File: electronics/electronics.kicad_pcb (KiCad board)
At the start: 2 copper layers, 50.3 x 40.6 mm, 24 parts, among them J3 EXTERNAL CONTROL, J4 POWER, J5 I2C BUS, J6 I2C BUS, J7 INPUT, J8 OUTPUT, U1 ProMicro

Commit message: Changed some art
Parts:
- removed svg2mod: G***, local:kv27v66mod
- removed svg2mod: G***, local:c6p-dev
- added c6p_logo: G***, local:c6p-dev, F.Cu at (120.1, 34.0)
- added kv_revision: G***, local:kv27v66mod, F.Cu at (110.5, 40.4)

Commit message: Last through hole
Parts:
- removed the REF** at (96.5, 54.4)
- removed the REF** at (138.2, 54.4)
- removed kv_revision: G***, local:kv27v66mod
- added REF**: MountingHole_3.2mm_M3_DIN965, MountingHole:MountingHole_3.2mm_M3_DIN965, F.Cu at (96.5, 54.4)
- R5, R6, R7, R8: footprint Resistor_THT:R_Axial_DIN0204_L3.6mm_D1.6mm_P1.90mm_Vertical -> Resistor_THT:R_Axial_DIN0204_L3.6mm_D1.6mm_P2.54mm_Vertical
- REF**: value MountingHole_3.2mm_M3 -> MountingHole_3.2mm_M3_DIN965; footprint MountingHole:MountingHole_3.2mm_M3 -> MountingHole:MountingHole_3.2mm_M3_DIN965
- moved J8 13.2 mm to (131.3, 50.5), turned to 0 degrees
- moved R8 12.9 mm to (135.6, 22.9)
- moved C4 9.88 mm to (140.0, 28.4)
- moved C1 8.20 mm to (129.3, 36.1)
- moved C2 8.20 mm to (134.1, 36.1)
- moved c6p_logo 7.16 mm to (113.8, 37.3)
- moved R7 4.35 mm to (125.0, 19.8)
- moved R6 2.62 mm to (122.2, 21.8)
- moved R3 2.40 mm to (118.4, 53.8), turned to 180 degrees
- moved J6 1.80 mm to (124.7, 50.0), turned to 270 degrees
- moved R5 1.30 mm to (119.4, 23.9)
- moved R1 1.30 mm to (110.5, 53.8)
- moved C3 0.76 mm to (135.6, 28.4)
- moved U1 0.76 mm to (109.2, 37.3)
- moved J3 0.51 mm to (112.3, 22.4)
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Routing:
- net GIN: track 31.3 -> 19.1 mm
- net RIN: track 26.7 -> 16.6 mm
- net ROUT: track 17.5 -> 10.3 mm
- net BIN: track 17.7 -> 13.8 mm
- net SYNCIN: track 15.4 -> 12.5 mm
- net BOUT: track 15.1 -> 17.4 mm
- net Net-(J6-Pad1): track 8.57 -> 6.67 mm
- net SCL2: track 9.36 -> 10.8 mm
- net RESET: track 18.5 -> 19.8 mm
- net SDA2: track 27.8 -> 26.5 mm
- net VCC: track 44.3 -> 45.5 mm
- net GOUT: track 10.6 -> 9.60 mm
- net Net-(J6-Pad2): track 7.79 -> 6.89 mm
- net SCL1: track 8.06 -> 7.30 mm
- net SDA1: track 8.04 -> 7.28 mm
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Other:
- board size 50.3 x 40.6 mm -> 51.6 x 41.1 mm
- net class Default: clearance 0.4 -> 0.6; trace_width 0.4 -> 0.8
- rule trace_clearance: 0.4 -> 0.6

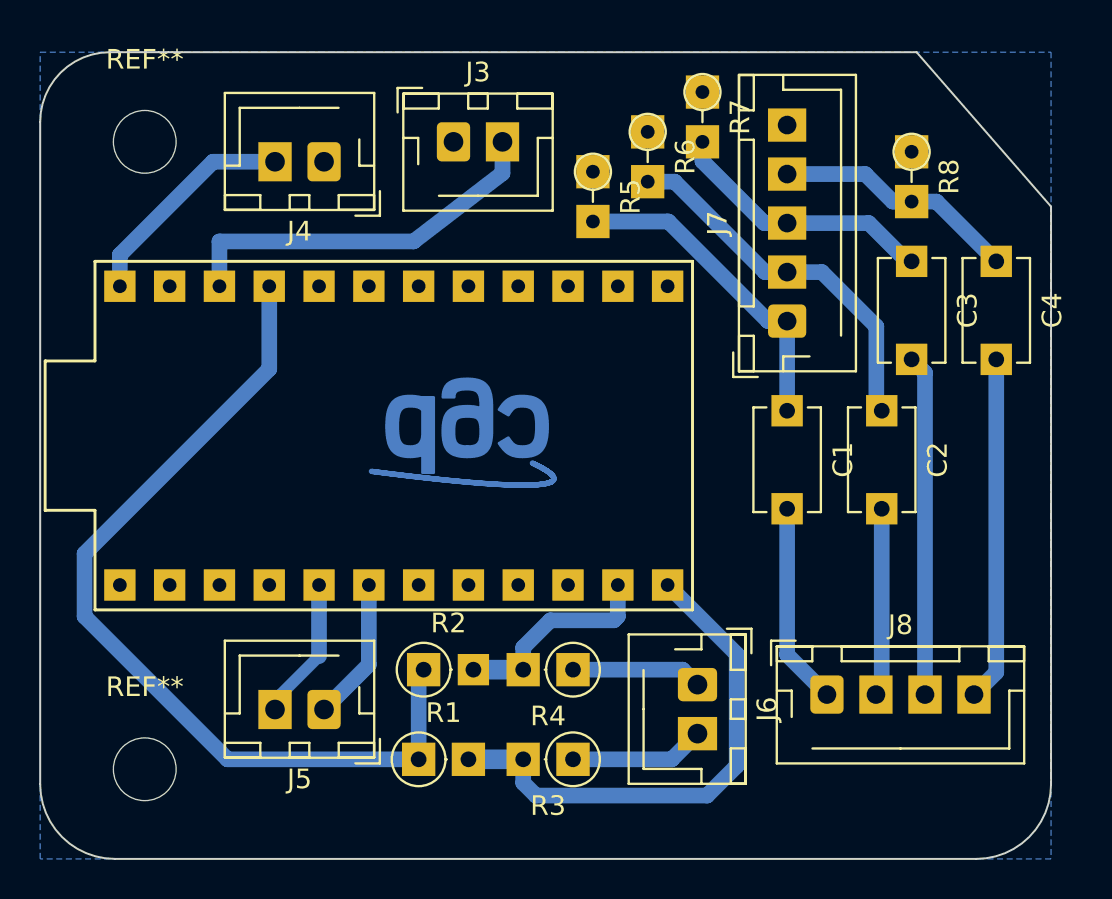
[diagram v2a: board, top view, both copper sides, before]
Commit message: Encoder support
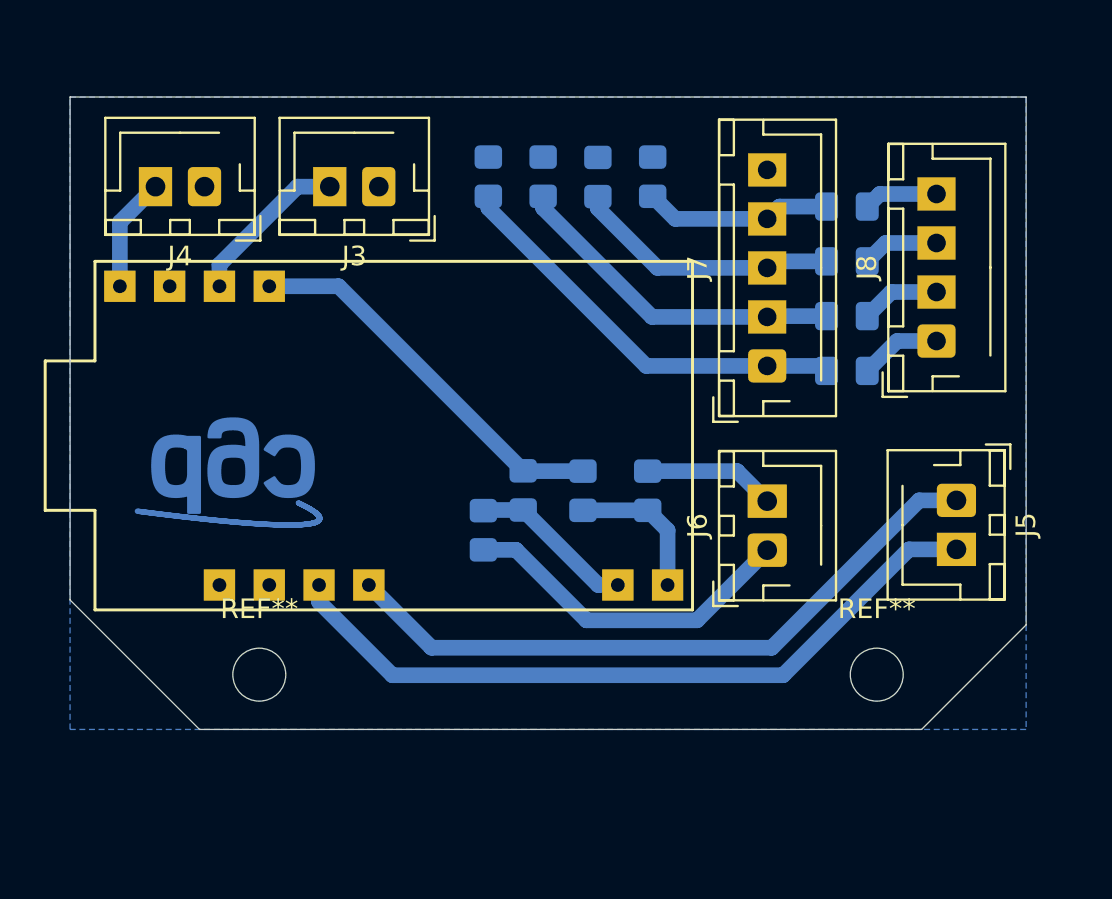
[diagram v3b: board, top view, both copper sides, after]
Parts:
- removed the REF** at (96.5, 22.4)
- removed the REF** at (96.5, 54.4)
- added ?: , , F.Cu at (100.3, 51.6)
- added REF**: MountingHole_2.7mm_M2.5_DIN965, MountingHole:MountingHole_2.7mm_M2.5_DIN965, F.Cu at (133.9, 49.5)
- added REF**: MountingHole_2.7mm_M2.5_DIN965, MountingHole:MountingHole_2.7mm_M2.5_DIN965, F.Cu at (102.4, 49.5)
- C1, C2, C3, C4: footprint Capacitor_THT:C_Disc_D5.1mm_W3.2mm_P5.00mm -> Capacitor_SMD:C_0805_2012Metric_Pad1.18x1.45mm_HandSolder; moved to B.Cu
- R1, R2, R3, R4: footprint Resistor_THT:R_Axial_DIN0207_L6.3mm_D2.5mm_P2.54mm_Vertical -> Resistor_SMD:R_0805_2012Metric_Pad1.20x1.40mm_HandSolder; moved to B.Cu
- R5, R6, R7, R8: footprint Resistor_THT:R_Axial_DIN0204_L3.6mm_D1.6mm_P2.54mm_Vertical -> Resistor_SMD:R_0805_2012Metric_Pad1.20x1.40mm_HandSolder; moved to B.Cu
- moved J5 34.0 mm to (137.9, 40.6), turned to 270 degrees
- moved J8 18.9 mm to (136.9, 32.5), turned to 90 degrees
- moved R1 16.1 mm to (118.9, 40.1), turned to 270 degrees
- moved R3 14.2 mm to (122.2, 40.1), turned to 270 degrees
- moved R8 13.3 mm to (122.4, 24.1)
- moved c6p_logo 12.1 mm to (101.9, 39.4)
- moved R2 10.5 mm to (115.8, 40.1), turned to 270 degrees
- moved R4 8.45 mm to (113.8, 42.2), turned to 90 degrees
- moved C4 8.12 mm to (132.3, 25.7), turned to 0 degrees
- moved J6 7.73 mm to (128.3, 43.2), turned to 90 degrees
- moved R7 6.87 mm to (119.6, 24.1)
- moved J4 6.23 mm to (99.6, 24.6)
- moved R6 5.80 mm to (116.8, 24.1)
- moved R5 5.34 mm to (114.0, 24.1)
- moved C2 5.14 mm to (132.3, 31.2), turned to 0 degrees
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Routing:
- net SDA1: track 7.28 -> 37.6 mm
- net SCL1: track 7.30 -> 34.4 mm
- net VCC: track 45.5 -> 19.9 mm
- net SDA2: track 26.5 -> 7.53 mm
- net SYNCOUT: track 17.6 -> 3.80 mm
- net BOUT: track 17.4 -> 3.92 mm
- net RESET: track 19.8 -> 8.38 mm
- net Net-(J6-Pad1): track 6.67 -> 17.4 mm
- net ROUT: track 10.3 -> 4.17 mm
- net RAW: track 11.5 -> 5.83 mm
- net GOUT: track 9.60 -> 4.04 mm
- net RIN: track 16.6 -> 21.3 mm
- net SYNCIN: track 12.5 -> 9.63 mm
- net SCL2: track 10.8 -> 8.46 mm
- net GIN: track 19.1 -> 17.4 mm
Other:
- board size 51.6 x 41.1 mm -> 48.8 x 32.3 mm
